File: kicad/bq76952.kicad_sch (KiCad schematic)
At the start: 82 parts, among them Q1 FCX495TA, U4 BQ76952

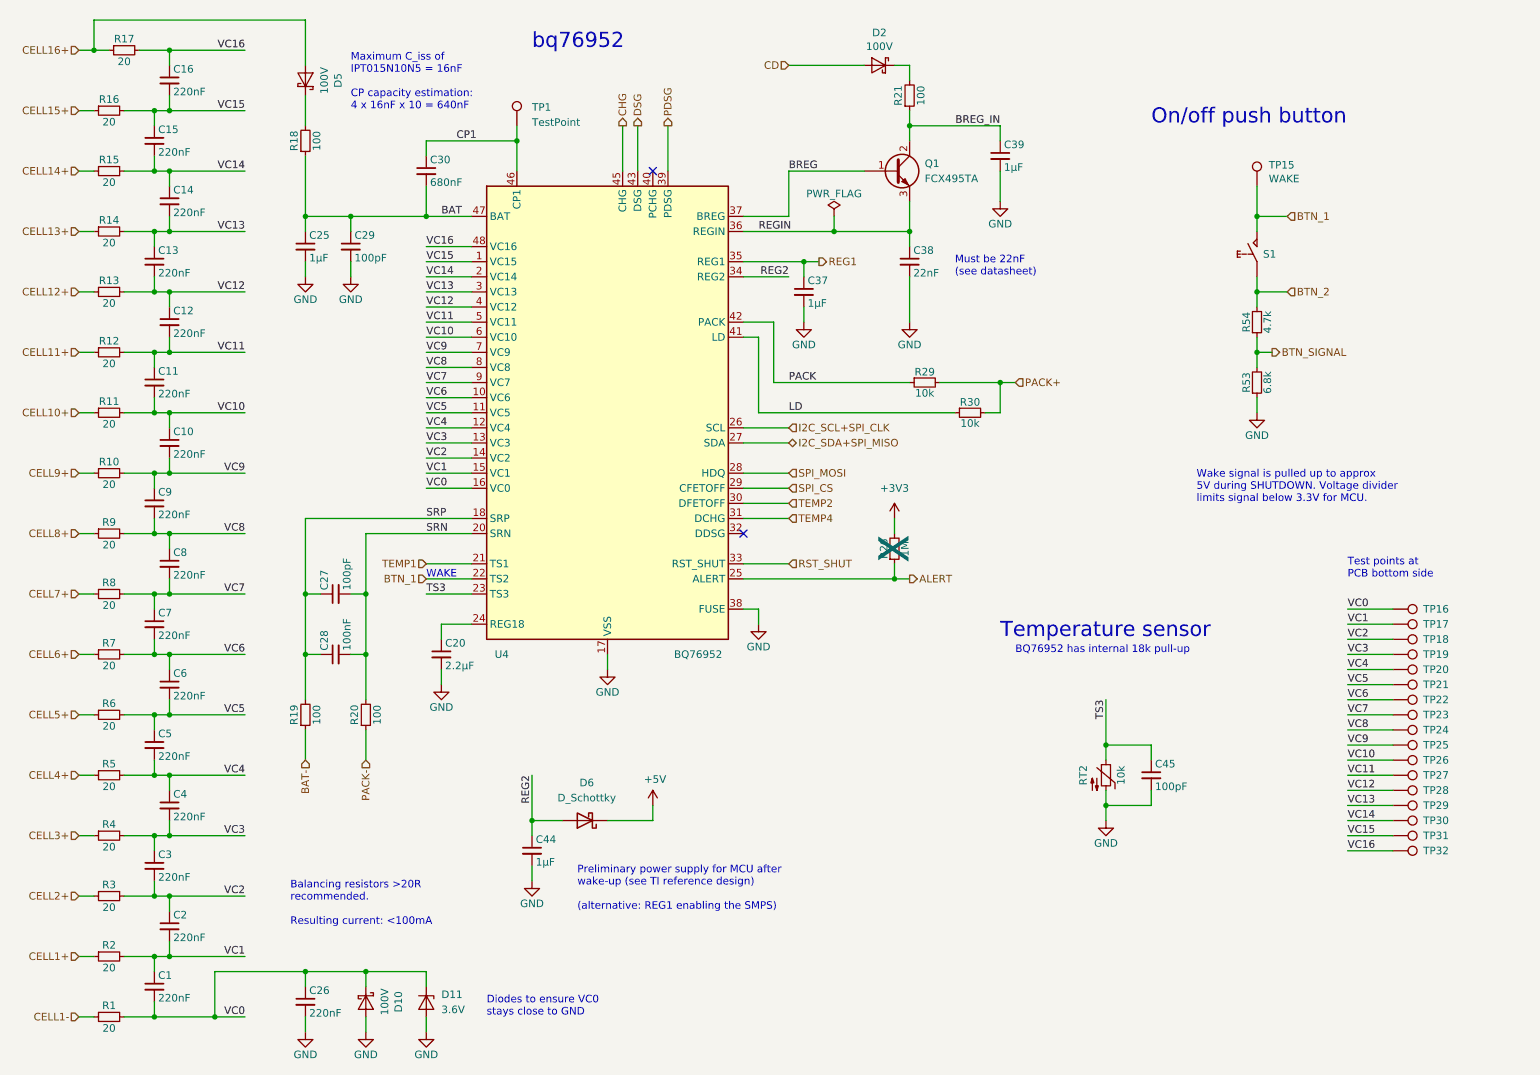
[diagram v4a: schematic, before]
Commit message: Major update for BMS C1 v0.3
This commit contains major updates of the PCB after the first prototype
build-up and testing. Changes include:

- Single PCB instead of stacked PCBs to simplify design and reduce cost.
- STM32 MCU was removed due to supply shortage. Only ESP32-C3 supported.
- Custom connectors replaced with off-the-shelf Würth Power Elements.
- 5V power rail removed to simplify design (CAN runs on 3V3 transceiver).
- Larger Shunt with improved footprint.
- Optimized layout to reduce distance between IC and shunt.
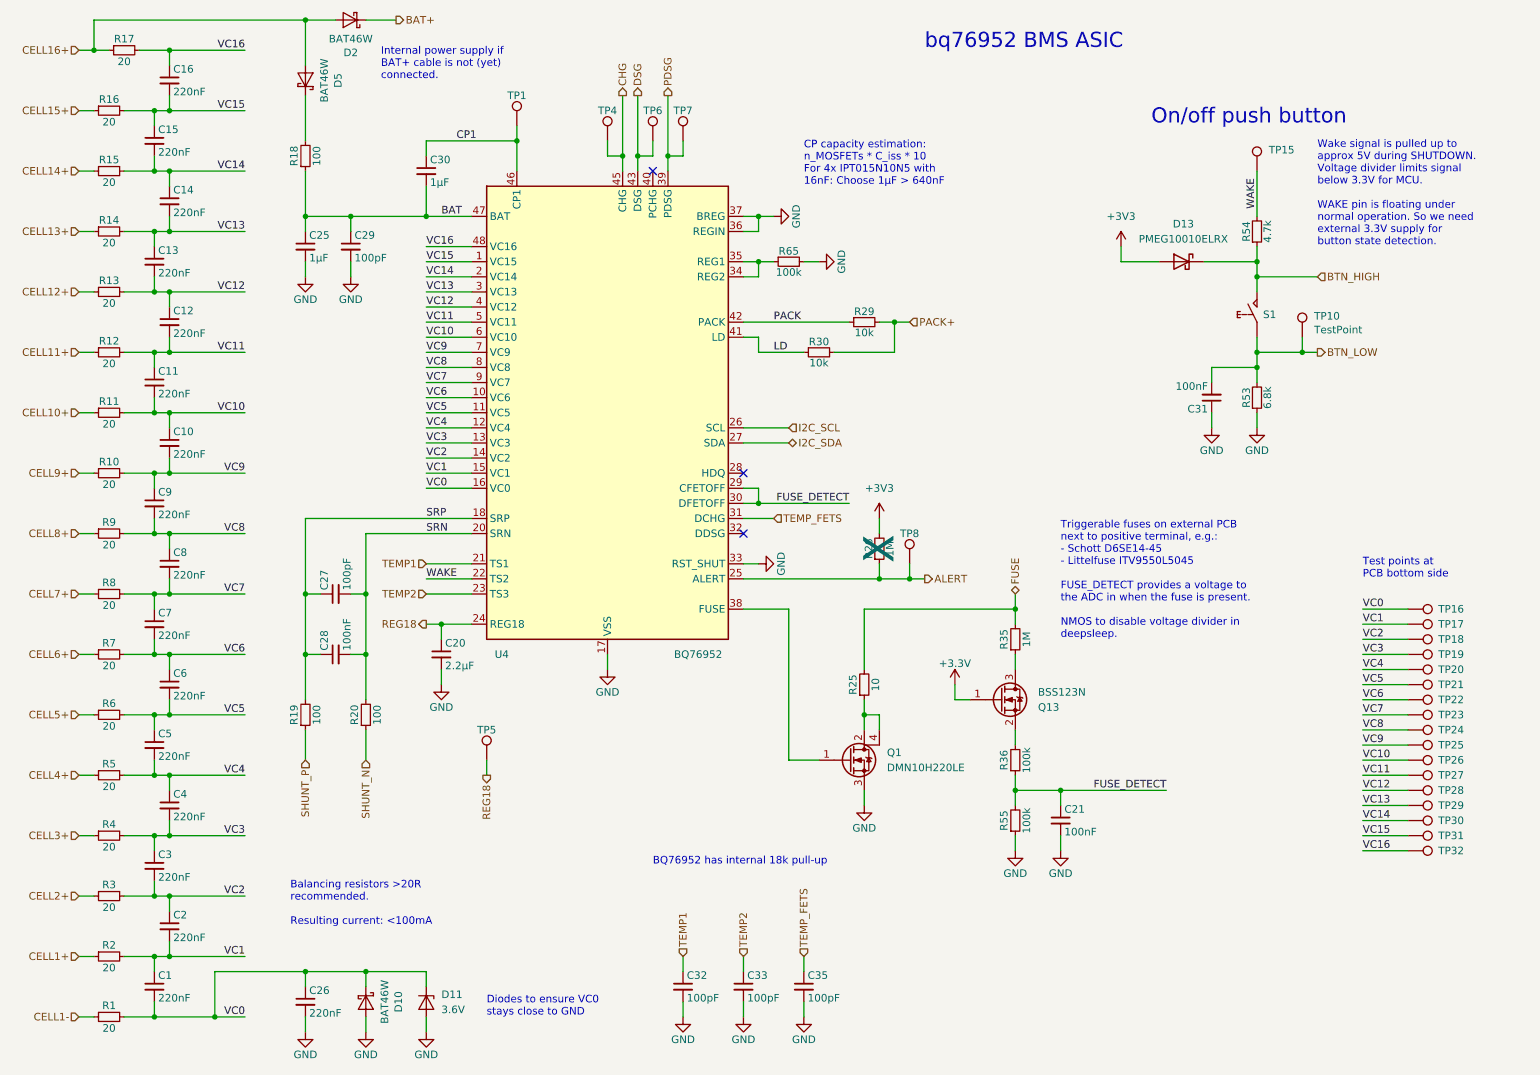
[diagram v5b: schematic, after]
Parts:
- removed C37, C39, C44: 1µF, LibreSolar:C_0603_1608, symbol LibreSolar:C
- removed C38: 22nF, LibreSolar:C_0603_1608, symbol LibreSolar:C
- removed D6: D_Schottky, Diode_SMD:D_SOD-123F, symbol Device:D_Schottky
- removed Q1: FCX495TA, Package_TO_SOT_SMD:SOT-89-3, symbol Device:Q_NPN_BCE
- removed R21: 100, LibreSolar:R_1206_3216, symbol LibreSolar:R
- removed RT2: 10k, LibreSolar:R_0603_1608, symbol LibreSolar:R_NTC
- added C21, C31: 100nF, LibreSolar:C_0603_1608, symbol LibreSolar:C
- added C33, C35: 100pF, LibreSolar:C_0603_1608, symbol LibreSolar:C
- added D13: PMEG10010ELRX, LibreSolar:D_SOD-123F, symbol Device:D_Schottky
- added Q1: DMN10H220LE, Package_TO_SOT_SMD:SOT-223, symbol Device:Q_NMOS_GDSD
- added Q13: BSS123N, LibreSolar:SOT-23, symbol Device:Q_NMOS_GSD
- added R25: 10, LibreSolar:R_1206_3216, symbol LibreSolar:R
- added R35: 1M, LibreSolar:R_0603_1608, symbol LibreSolar:R
- added R36, R55, R65: 100k, LibreSolar:R_0603_1608, symbol LibreSolar:R
- added TP10, TP4, TP5, TP6, TP7, TP8: TestPoint, TestPoint:TestPoint_Pad_D1.5mm, symbol Connector:TestPoint
- C28: Remarks (none) -> X7R, 100V
- C30: value 680nF -> 1µF; Remarks (none) -> 25V, X5R
- D10, D2, D5: value 100V -> BAT46W; footprint Diode_SMD:D_SOD-123 -> LibreSolar:D_SOD-123; Remarks (none) -> 100V
- D11: footprint Diode_SMD:D_SOD-123 -> LibreSolar:D_SOD-123
- S1: footprint LibreSolar:SW_SPST_6mm -> Button_Switch_SMD:SW_SPST_TL3305A
- TP15: value WAKE -> TestPoint
- TP16, TP17, TP18, TP19, TP20, TP21, TP22, TP23, TP24, TP25, TP26, TP27, TP28, TP29, TP30, TP31, TP32: footprint TestPoint:TestPoint_Pad_D1.5mm -> TestPoint:TestPoint_Pad_1.0x1.0mm
- renumbered C45 to C32
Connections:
- net BREG is gone; now on net GND: U4.37 (BREG)
- net CD is gone; now on net CELL16+: D2.2 (A)
- net REG2 is gone; now on an unnamed net: U4.34 (REG2)
- net REGIN is gone; now on net GND: U4.36 (REGIN)
- net RST_SHUT is gone; now on net GND: U4.33 (RST_SHUT)
- net +3V3: now also D13.2 (A), Q13.1 (G)
- net ALERT: now also TP8.1
- net CHG: now also TP4.1
- net DSG: now also TP6.1
- net GND: now also C21.2, C31.1, C33.2, C35.2, Q1.3 (S), R55.1, R65.2; no longer U4.38 (FUSE)
- net PDSG: now also TP7.1
- net TEMP1: now also C32.1
- net TEMP2: now also U4.23 (TS3), C33.1; no longer U4.30 (DFETOFF)
- net BAT+: now reaches D2.1 (K)
- net REG18: now reaches C20.1, U4.24 (REG18)
- net REG18: now also TP5.1
- net BAT- renamed SHUNT_P
- net BTN_1 renamed WAKE
- net WAKE: now also R54.2; no longer S1.2
- net BTN_2 renamed BTN_LOW
- net BTN_LOW: now also R53.2, C31.2, TP10.1; no longer R54.2
- net BTN_SIGNAL renamed BTN_HIGH
- net BTN_HIGH: now also S1.2, D13.1 (K); no longer R53.2
- net I2C_SCL+SPI_CLK renamed I2C_SCL
- net I2C_SDA+SPI_MISO renamed I2C_SDA
- net PACK- renamed SHUNT_N
- net REG1: no longer names the net of U4.35 (REG1)
- net REG1: now also R65.1
- net SPI_CS renamed FUSE_DETECT
- net FUSE_DETECT: now also U4.30 (DFETOFF), C21.1, R36.1, R55.2
- net SPI_MOSI: no longer names the net of U4.28 (HDQ)
- net TEMP4 renamed TEMP_FETS
- net TEMP_FETS: now also C35.1
- removed net TS3: C32.1, U4.23 (TS3)
- new net: Q13.2 (S), R36.2
- new net: Q13.3 (D), R35.1
- new net: Q1.1 (G), U4.38 (FUSE)
- new net: Q1.2 (D), Q1.4 (D), R25.1
- new net FUSE: R25.2, R35.2
- no-connect marks 2 -> 3
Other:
- note added: "CP capacity estimation: n_MOSFETs * C_iss * 10 For 4x IPT015N10N5 with 16nF: Choose 1µF > 640nF"
- note added: "Internal power supply if BAT+ cable is not (yet) connected."
- note added: "Triggerable fuses on external PCB next to positive terminal, e.g.: - Schott D6SE14-45 - Littelfuse ITV9550L5045 FUSE_DETECT provides a voltage to the ADC in when the fuse is present. NMOS to disable voltage divider in deepsleep."
- note added: "Wake signal is pulled up to approx 5V during SHUTDOWN. Voltage divider limits signal below 3.3V for MCU. WAKE pin is floating under normal operation. So we need external 3.3V supply for button state detection."
- note added: "bq76952 BMS ASIC"
- note removed: "Maximum C_iss of IPT015N10N5 = 16nF CP capacity estimation: 4 x 16nF x 10 = 640nF"
- note removed: "Must be 22nF (see datasheet)"
- note removed: "Preliminary power supply for MCU after wake-up (see TI reference design) (alternative: REG1 enabling the SMPS)"
- note removed: "Temperature sensor"
- note removed: "WAKE"
- note removed: "Wake signal is pulled up to approx 5V during SHUTDOWN. Voltage divider limits signal below 3.3V for MCU."
- note removed: "bq76952"
- title: BMS 16S Control Board -> Libre Solar BMS C1
- moved on the sheet: C32, R18, R26, R29, R30, R53, R54, S1, TP15, TP16, TP17, TP18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

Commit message: BOM updates with a few more alternative parts
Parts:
- D10, D2, D5: Remarks 100V -> Alternative: MCC BAT46WHE3-TP
- D13: Remarks (none) -> Alternative: Nexperia PMEG10030ELPX
- Q1: Remarks 100V, >2A -> 100V, >2A, Alternative: IRFM120ATF
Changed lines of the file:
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@@
       (effects (font (size 1.27 1.27)) hide)
     )
-    (property "Remarks" "100V" (id 6) (at 76.2 27.94 0)
+    (property "Remarks" "Alternative: MCC BAT46WHE3-TP" (id 6) (at 76.2 27.94 0)
       (effects (font (size 1.27 1.27)) hide)
     )
@@
       (effects (font (size 1.27 1.27)) hide)
     )
-    (property "Remarks" "100V" (id 6) (at 86.36 182.88 0)
+    (property "Remarks" "Alternative: MCC BAT46WHE3-TP" (id 6) (at 86.36 182.88 0)
       (effects (font (size 1.27 1.27)) hide)
     )
@@
       (effects (font (size 1.27 1.27)) hide)
     )
-    (property "Remarks" "100V" (id 6) (at 83.82 17.78 0)
+    (property "Remarks" "Alternative: MCC BAT46WHE3-TP" (id 6) (at 83.82 17.78 0)
       (effects (font (size 1.27 1.27)) hide)
     )
@@
       (effects (font (size 1.27 1.27)) hide)
     )
-    (property "Remarks" "100V, >2A" (id 6) (at 167.64 142.24 0)
+    (property "Remarks" "100V, >2A, Alternative: IRFM120ATF" (id 6) (at 167.64 142.24 0)
       (effects (font (size 1.27 1.27)) hide)
     )
@@
       (effects (font (size 1.27 1.27)) hide)
     )
+    (property "Remarks" "Alternative: Nexperia PMEG10030ELPX" (id 6) (at 223.52 58.42 0)
+      (effects (font (size 1.27 1.27)) hide)
+    )

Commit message: Add ESP32-C3 and switch part numbers
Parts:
- S1: Manufacturer (none) -> E-Switch; PartNumber (none) -> TL3305AF160QG
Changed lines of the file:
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@@
     )
     (property "Datasheet" "" (id 3) (at 236.22 67.31 0))
+    (property "Manufacturer" "E-Switch" (id 4) (at 236.22 67.31 0)
+      (effects (font (size 1.27 1.27)) hide)
+    )
+    (property "PartNumber" "TL3305AF160QG" (id 5) (at 236.22 67.31 0)
+      (effects (font (size 1.27 1.27)) hide)
+    )
     (pin "1")
     (pin "2")
